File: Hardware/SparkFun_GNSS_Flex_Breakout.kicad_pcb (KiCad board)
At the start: 4 copper layers, 63.5 x 50.8 mm, 210 parts, among them J1 microSD_Friction, J10 USB_C_Receptacle, J11 Conn_02x10, J12 Conn_02x10, J13 JST_Locking_6, J14 Qwiic_Vertical, J15 Legend: GNSS Flex, J2 SMA_Edge, J3 Conn_01x15, J4 Conn_01x18, J5 JST_Locking_6, J6 SMA_Edge, J7 USB_C_Receptacle, J8 U.FL, J9 U.FL, U1 RT9080-3.3, U2 CH342F, U3 74HC4066BQ, U4 AP7361C-3.3V, U5 74HC4066BQ

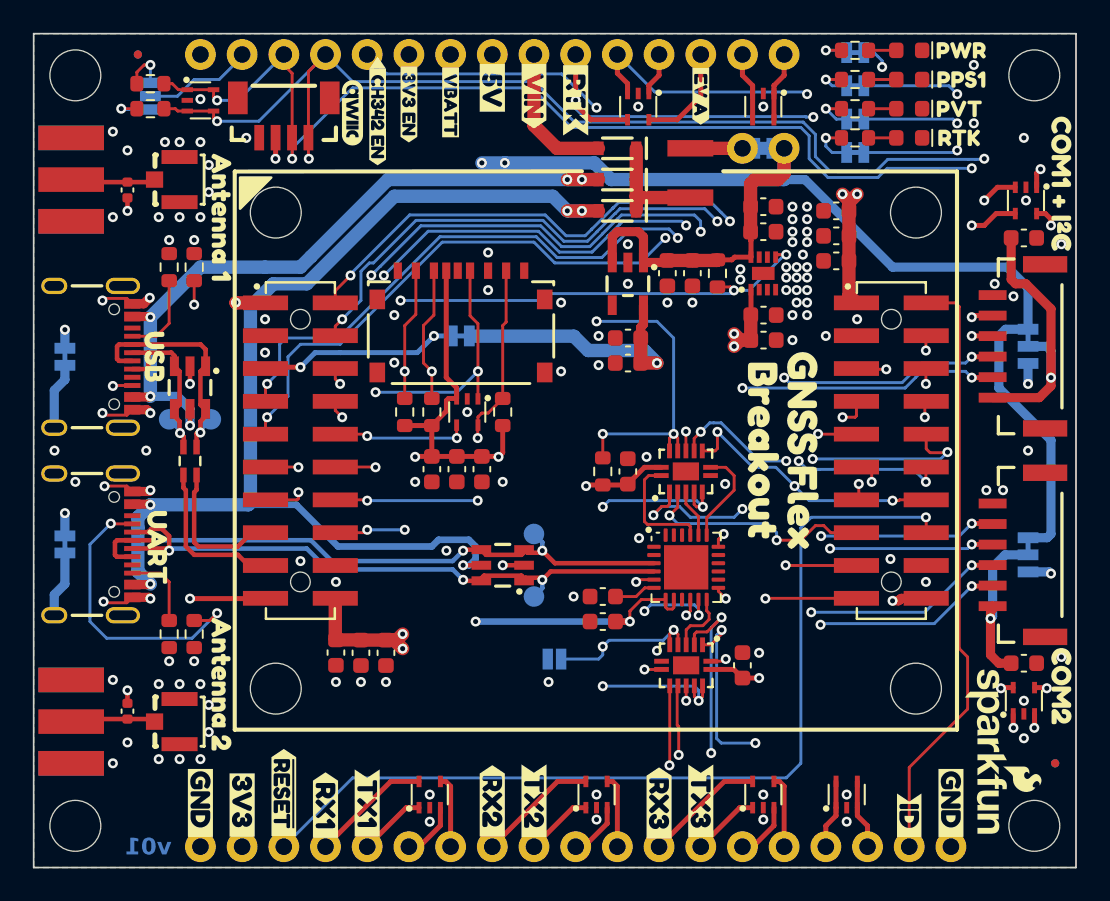
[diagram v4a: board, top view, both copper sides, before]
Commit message: PCB v02 - with corrected regulator footprint
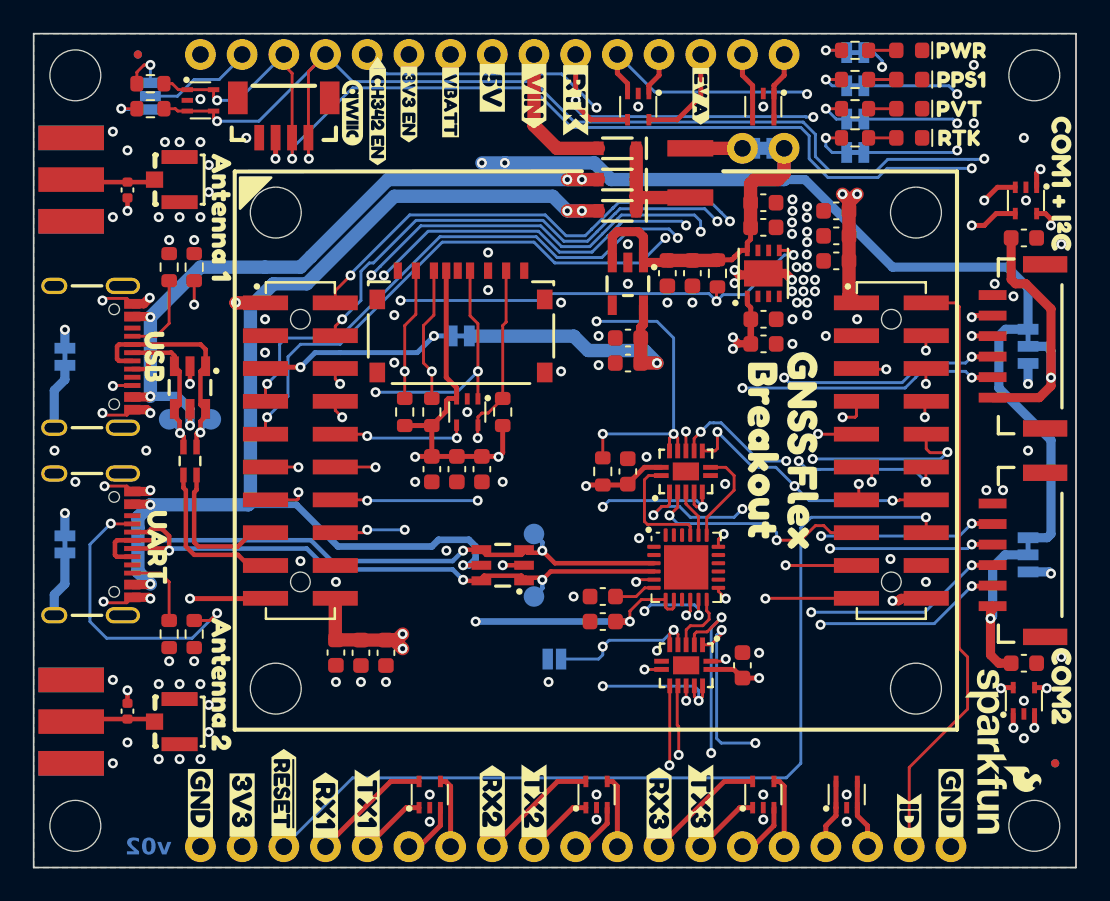
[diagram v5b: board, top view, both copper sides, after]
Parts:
- J2, J6: value SMA_Edge -> Val**
- J4: value Conn_01x18 -> Conn_01x19
- J8, J9: value U.FL -> Val**
- TR2: value RFCMF1220100M4T -> Val**
- U4: footprint SparkFun-Semiconductor-Standard:DFN-8_3x3mm -> SparkFun-Semiconductor-Standard:DFN-8_3x3mm_P0.65mm_EP2.25x1.5mm
- moved C16 0.27 mm to (160.0, 85.5)
- moved C17 0.25 mm to (160.0, 91.1)
- moved C15 0.24 mm to (160.0, 84.0)
- moved C18 0.23 mm to (160.0, 92.6)
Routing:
- net GND: track 18.9 -> 22.7 mm, vias 127 -> 126
- net 3V3_EN: track 41.7 -> 42.6 mm
- net 3.3V: track 68.0 -> 68.6 mm
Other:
- board text added: "v02"
- board text removed: "v01"

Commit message: v10 PCB - correct PVT and RTK LEDs, and VBACKUP silk
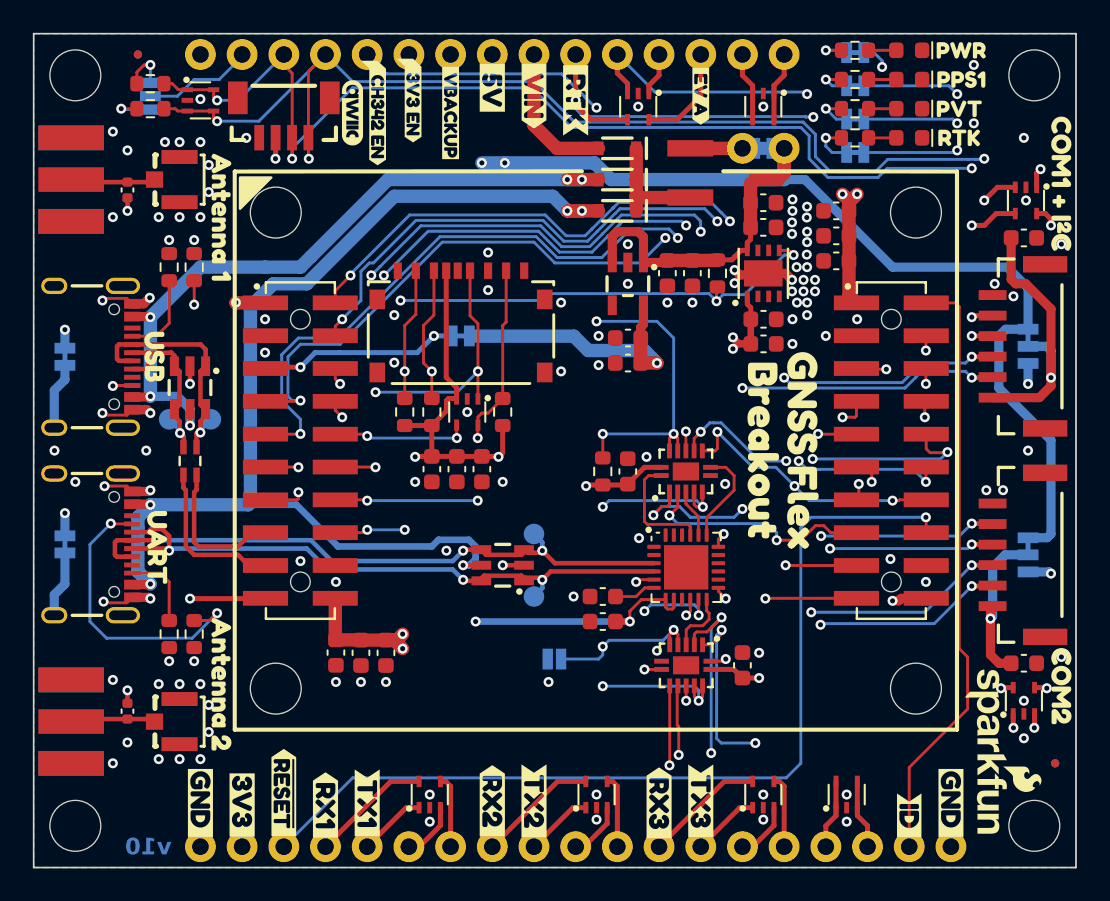
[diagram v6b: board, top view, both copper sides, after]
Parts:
- removed kibuzzard-67EFDDCD: G***, kibuzzard-67EFDDCD
- removed kibuzzard-67F7ADB8: G***, kibuzzard-67F7ADB8
- removed kibuzzard-67F7B6D2: G***, kibuzzard-67F7B6D2
- added kibuzzard-682202FA: G***, kibuzzard-682202FA, F.Cu at (141.0, 78.5)
- added kibuzzard-6822032F: G***, kibuzzard-6822032F, B.Cu at (141.6, 87.2)
- added kibuzzard-68220336: G***, kibuzzard-68220336, B.Cu at (141.0, 79.1)
- J2, J6: value Val** -> SMA_Edge
- J8, J9: value Val** -> U.FL
- TR2: value Val** -> RFCMF1220100M4T
- moved kibuzzard-67F7B6D7 0.25 mm to (138.7, 78.0)
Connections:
- J11 pad 7: PVT_LED -> RTK_LED
- J11 pad 9: RTK_LED -> PVT_LED
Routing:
- net PVT_LED: track 76.1 -> 79.8 mm
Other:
- board text added: "Material: TG135"
- board text added: "v10"
- board text removed: "Material: TG155"
- board text removed: "v02"
